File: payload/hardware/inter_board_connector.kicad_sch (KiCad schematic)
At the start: 1 part, among them J10 Conn_02x20_Counter_Clockwise

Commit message: do some layout, route camera differential pairs, add inter-board connector, pick parts for CAN
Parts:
- J10: footprint footprints:SAMTEC_ERM8-020-X-X-DV -> Connector_Samtec_EdgeRate:Samtec_ERF8-020-XX.X-DV_2x20_P0.8mm_Socket
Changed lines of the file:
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@@
 			)
 		)
-		(property "Footprint" "footprints:SAMTEC_ERM8-020-X-X-DV"
+		(property "Footprint" "Connector_Samtec_EdgeRate:Samtec_ERF8-020-XX.X-DV_2x20_P0.8mm_Socket"
 			(at 144.78 99.06 0)
 			(hide yes)

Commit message: did it not save again?
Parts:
- J10: value Conn_02x20_Counter_Clockwise -> Conn_02x20_Odd_Even; footprint Connector_Samtec_EdgeRate:Samtec_ERF8-020-XX.X-DV_2x20_P0.8mm_Socket -> (none); symbol Connector_Generic:Conn_02x20_Counter_Clockwise -> Connector_Generic:Conn_02x20_Odd_Even
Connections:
- net EPS_OBC_RESET: now also J10.23 (Pin_23); no longer J10.12 (Pin_12)
- net EPS_PGOOD: now also J10.21 (Pin_21); no longer J10.11 (Pin_11)
- net GND: now also J10.1 (Pin_1), J10.19 (Pin_19), J10.2 (Pin_2), J10.39 (Pin_39); no longer J10.01 (Pin_1), J10.10 (Pin_10), J10.21 (Pin_21), J10.31 (Pin_31)
- net OBC_EPS_RESET: now also J10.25 (Pin_25); no longer J10.13 (Pin_13)
- net OBC_HEARTBEAT: now also J10.27 (Pin_27); no longer J10.14 (Pin_14)
- net RAIL_1_VOUT: now also J10.3 (Pin_3), J10.4 (Pin_4); no longer J10.02 (Pin_2), J10.39 (Pin_39)
- net RAIL_2_VOUT: now also J10.5 (Pin_5), J10.6 (Pin_6); no longer J10.03 (Pin_3), J10.38 (Pin_38)
- net RAIL_3_VOUT: now also J10.7 (Pin_7), J10.8 (Pin_8); no longer J10.04 (Pin_4), J10.37 (Pin_37)
- net RAIL_4_VOUT: now also J10.10 (Pin_10), J10.9 (Pin_9); no longer J10.05 (Pin_5), J10.36 (Pin_36)
- net RAIL_5_VOUT: now also J10.11 (Pin_11), J10.12 (Pin_12); no longer J10.06 (Pin_6), J10.35 (Pin_35)
- net RAIL_6_VOUT: now also J10.13 (Pin_13), J10.14 (Pin_14); no longer J10.07 (Pin_7), J10.34 (Pin_34)
- net RAIL_7_VOUT: now also J10.15 (Pin_15), J10.16 (Pin_16); no longer J10.08 (Pin_8), J10.33 (Pin_33)
- net RAIL_8_VOUT: now also J10.17 (Pin_17), J10.18 (Pin_18); no longer J10.09 (Pin_9), J10.32 (Pin_32)
- net SYSTEM_AUX_UART_RX: now also J10.36 (Pin_36); no longer J10.23 (Pin_23)
- net SYSTEM_AUX_UART_TX: now also J10.38 (Pin_38); no longer J10.22 (Pin_22)
- net SYSTEM_MAIN_UART_RX: now also J10.35 (Pin_35); no longer J10.18 (Pin_18)
- net SYSTEM_MAIN_UART_TX: now also J10.37 (Pin_37); no longer J10.19 (Pin_19)
- net CAN_MAIN-: now reaches J10.24 (Pin_24)
- net CAN_AUX+: now reaches J10.26 (Pin_26)
- net CAN_AUX-: now reaches J10.28 (Pin_28)
- new net CAN_MAIN+: J10.22 (Pin_22)
- no-connect marks 10 -> 6
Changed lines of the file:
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@@
-	)
-	(no_connect
-		(at 152.4 101.6)
-	)
-	(no_connect
-		(at 152.4 109.22)
 	)
 	(no_connect
@@
 	)
 	(no_connect
-		(at 152.4 106.68)
-	)
-	(no_connect
 		(at 152.4 116.84)
 	)
@@
 	)
 	(no_connect
-		(at 152.4 104.14)
-	)
-	(no_connect
 		(at 152.4 111.76)
 	)
@@
 	(wire
 		(pts
+			(xy 152.4 101.6) (xy 165.1 101.6)
+		)
+		(stroke
+			(width 0)
+			(type default)
+		)
+	)
+	(wire
+		(pts
 			(xy 165.1 99.06) (xy 152.4 99.06)
 		)
@@
 	(wire
 		(pts
+			(xy 152.4 109.22) (xy 165.1 109.22)
+		)
+		(stroke
+			(width 0)
+			(type default)
+		)
+	)
+	(wire
+		(pts
 			(xy 127 99.06) (xy 139.7 99.06)
 		)
@@
 	(wire
 		(pts
+			(xy 152.4 106.68) (xy 165.1 106.68)
+		)
+		(stroke
+			(width 0)
+			(type default)
+		)
+	)
+	(wire
+		(pts
 			(xy 152.4 96.52) (xy 165.1 96.52)
 		)
@@
 		(pts
 			(xy 127 121.92) (xy 139.7 121.92)
+		)
+		(stroke
+			(width 0)
+			(type default)
+		)
+	)
+	(wire
+		(pts
+			(xy 152.4 104.14) (xy 165.1 104.14)
 		)
 		(stroke
@@
 		)
 	)
+	(hierarchical_label "CAN_MAIN+"
+		(shape bidirectional)
+		(at 165.1 101.6 0)
+		(effects
+			(font
+				(size 1.27 1.27)
+			)
+			(justify left)
+		)
+	)
 	(hierarchical_label "RAIL_2_VOUT"
 		(shape input)
@@
 		)
 	)
+	(hierarchical_label "CAN_AUX-"
+		(shape bidirectional)
+		(at 165.1 109.22 0)
+		(effects
+			(font
+				(size 1.27 1.27)
+			)
+			(justify left)
+		)
+	)
+	(hierarchical_label "CAN_AUX+"
+		(shape bidirectional)
+		(at 165.1 106.68 0)
+		(effects
+			(font
+				(size 1.27 1.27)
+			)
+			(justify left)
+		)
+	)
 	(hierarchical_label "SYSTEM_AUX_UART_RX"
 		(shape input)
@@
 		(shape input)
 		(at 165.1 121.92 0)
+		(effects
+			(font
+				(size 1.27 1.27)
+			)
+			(justify left)
+		)
+	)
+	(hierarchical_label "CAN_MAIN-"
+		(shape bidirectional)
+		(at 165.1 104.14 0)
 		(effects
 			(font
@@
 	)
 	(symbol
-		(lib_id "Connector_Generic:Conn_02x20_Counter_Clockwise")
+		(lib_id "Connector_Generic:Conn_02x20_Odd_Even")
 		(at 144.78 99.06 0)
 		(unit 1)
@@
 			)
 		)
-		(property "Value" "Conn_02x20_Counter_Clockwise"
+		(property "Value" "Conn_02x20_Odd_Even"
 			(at 146.05 72.39 0)
 			(show_name no)
@@
 			)
 		)
-		(property "Footprint" "Connector_Samtec_EdgeRate:Samtec_ERF8-020-XX.X-DV_2x20_P0.8mm_Socket"
+		(property "Footprint" ""
 			(at 144.78 99.06 0)
 			(hide yes)
@@
 			)
 		)
-		(property "Description" "Generic connector, double row, 02x20, counter clockwise pin numbering scheme (similar to DIP package numbering), script generated (kicad-library-utils/schlib/autogen/connector/)"
+		(property "Description" "Generic connector, double row, 02x20, odd/even pin numbering scheme (row 1 odd numbers, row 2 even numbers), script generated (kicad-library-utils/schlib/autogen/connector/)"
 			(at 144.78 99.06 0)
 			(hide yes)
@@
 		(pin "31"
 		)
-		(pin "03"
+		(pin "5"
 		)
 		(pin "12"
@@
 		(pin "15"
 		)
-		(pin "07"
+		(pin "8"
 		)
 		(pin "21"
 		)
-		(pin "08"
+		(pin "7"
 		)
 		(pin "18"
@@
 		(pin "23"
 		)
-		(pin "04"
+		(pin "4"
 		)
 		(pin "25"
@@
 		(pin "30"
 		)
-		(pin "06"
+		(pin "2"
 		)
 		(pin "28"
@@
 		(pin "34"
 		)
-		(pin "05"
-		)
-		(pin "02"
-		)
-		(pin "09"
+		(pin "9"
+		)
+		(pin "6"
+		)
+		(pin "3"
 		)
 		(pin "26"
 		)
-		(pin "01"
+		(pin "1"
 		)
 		(pin "35"

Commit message: add part of a motor driver
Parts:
- J10: footprint (none) -> Connector_Samtec_EdgeRate:Samtec_ERF8-020-XX.X-DV_2x20_P0.8mm_Socket
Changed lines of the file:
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@@
 			)
 		)
-		(property "Footprint" ""
+		(property "Footprint" "Connector_Samtec_EdgeRate:Samtec_ERF8-020-XX.X-DV_2x20_P0.8mm_Socket"
 			(at 144.78 99.06 0)
 			(hide yes)
@@
 			(at 144.78 99.06 0)
 			(hide yes)
+			(show_name no)
+			(do_not_autoplace no)
+			(effects
+				(font
+					(size 1.27 1.27)
+				)
+			)
+		)
+		(property "Availability" ""
+			(at 144.78 99.06 0)
+			(hide yes)
+			(show_name no)
+			(do_not_autoplace no)
+			(effects
+				(font
+					(size 1.27 1.27)
+				)
+			)
+		)
+		(property "Check_prices" ""
+			(at 144.78 99.06 0)
+			(hide yes)
+			(show_name no)
+			(do_not_autoplace no)
+			(effects
+				(font
+					(size 1.27 1.27)
+				)
+			)
+		)
+		(property "Description_1" ""
+			(at 144.78 99.06 0)
+			(hide yes)
+			(show_name no)
+			(do_not_autoplace no)
+			(effects
+				(font
+					(size 1.27 1.27)
+				)
+			)
+		)
+		(property "MANUFACTURER" ""
+			(at 144.78 99.06 0)
+			(hide yes)
+			(show_name no)
+			(do_not_autoplace no)
+			(effects
+				(font
+					(size 1.27 1.27)
+				)
+			)
+		)
+		(property "MANUFACTURER_PART_NUMBER" ""
+			(at 144.78 99.06 0)
+			(hide yes)
+			(show_name no)
+			(do_not_autoplace no)
+			(effects
+				(font
+					(size 1.27 1.27)
+				)
+			)
+		)
+		(property "MAXIMUM_PACKAGE_HEIGHT" ""
+			(at 144.78 99.06 0)
+			(hide yes)
+			(show_name no)
+			(do_not_autoplace no)
+			(effects
+				(font
+					(size 1.27 1.27)
+				)
+			)
+		)
+		(property "MF" ""
+			(at 144.78 99.06 0)
+			(hide yes)
+			(show_name no)
+			(do_not_autoplace no)
+			(effects
+				(font
+					(size 1.27 1.27)
+				)
+			)
+		)
+		(property "MFR_NAME" ""
+			(at 144.78 99.06 0)
+			(hide yes)
+			(show_name no)
+			(do_not_autoplace no)
+			(effects
+				(font
+					(size 1.27 1.27)
+				)
+			)
+		)
+		(property "MP" ""
+			(at 144.78 99.06 0)
+			(hide yes)
+			(show_name no)
+			(do_not_autoplace no)
+			(effects
+				(font
+					(size 1.27 1.27)
+				)
+			)
+		)
+		(property "PARTREV" ""
+			(at 144.78 99.06 0)
+			(hide yes)
+			(show_name no)
+			(do_not_autoplace no)
+			(effects
+				(font
+					(size 1.27 1.27)
+				)
+			)
+		)
+		(property "Package" ""
+			(at 144.78 99.06 0)
+			(hide yes)
+			(show_name no)
+			(do_not_autoplace no)
+			(effects
+				(font
+					(size 1.27 1.27)
+				)
+			)
+		)
+		(property "Price" ""
+			(at 144.78 99.06 0)
+			(hide yes)
+			(show_name no)
+			(do_not_autoplace no)
+			(effects
+				(font
+					(size 1.27 1.27)
+				)
+			)
+		)
+		(property "STANDARD" ""
+			(at 144.78 99.06 0)
+			(hide yes)
+			(show_name no)
+			(do_not_autoplace no)
+			(effects
+				(font
+					(size 1.27 1.27)
+				)
+			)
+		)
+		(property "SnapEDA_Link" ""
+			(at 144.78 99.06 0)
+			(hide yes)

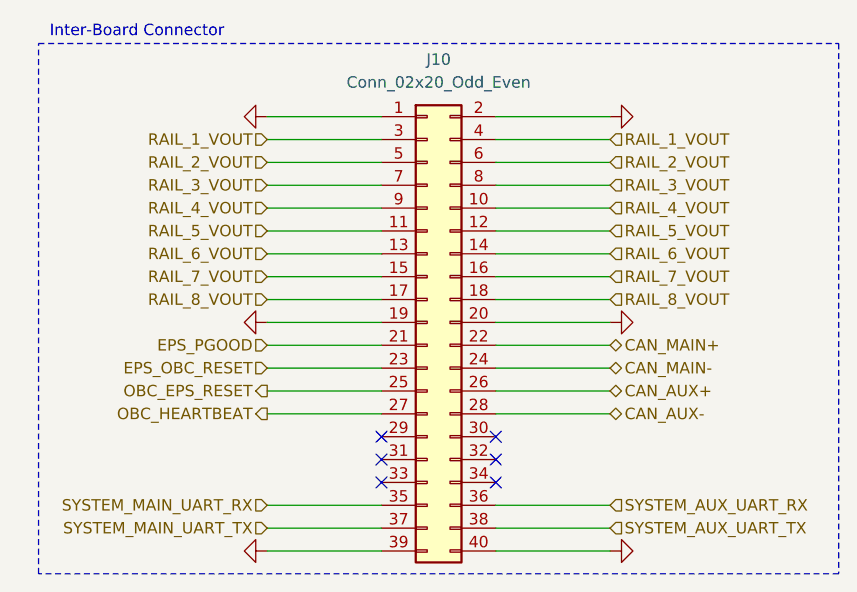
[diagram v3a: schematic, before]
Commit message: motor driver schematic, work on high speed routing
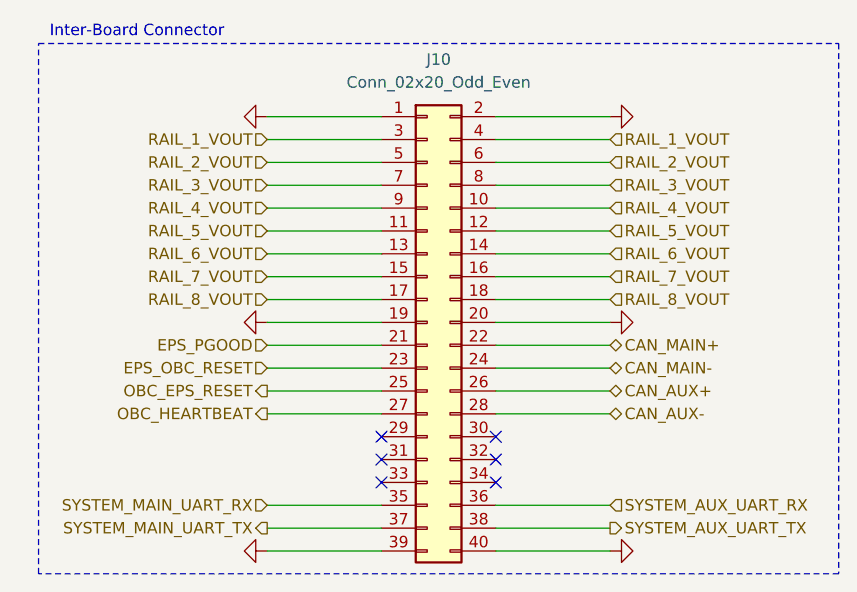
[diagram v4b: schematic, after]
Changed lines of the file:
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@@
 	)
 	(hierarchical_label "SYSTEM_AUX_UART_TX"
-		(shape input)
+		(shape output)
 		(at 165.1 121.92 0)
 		(effects
@@
 	)
 	(hierarchical_label "SYSTEM_MAIN_UART_TX"
-		(shape input)
+		(shape output)
 		(at 127 121.92 180)
 		(effects

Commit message: add digikey part numbers
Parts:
- J10: Digikey (none) -> 612-ERF8-020-09.0-L-DV-TRCT-ND
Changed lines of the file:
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@@
+			)
+		)
+		(property "Digikey" "612-ERF8-020-09.0-L-DV-TRCT-ND"
+			(at 144.78 99.06 0)
+			(hide yes)
+			(show_name no)
+			(do_not_autoplace no)
+			(effects
+				(font
+					(size 1.27 1.27)
+				)
 			)
 		)
